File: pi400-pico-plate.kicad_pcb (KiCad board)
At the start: 2 copper layers, 44 x 52.5 mm, 7 parts, among them J1 2.54mm socket RA, J2 2.54mm header, J3 2.54mm header, J4 2.54mm header, J5 2.54mm header, SW1 PTS815, U1 Pico

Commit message: Start rev B changes -- make UART jumpers cut-link, remove aux GND header
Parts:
- removed J5: 2.54mm header, Connector_PinHeader_2.54mm:PinHeader_2x01_P2.54mm_Vertical
- J2, J4: value 2.54mm header -> 2.54mm jumper cut-link; footprint Connector_PinHeader_2.54mm:PinHeader_2x01_P2.54mm_Vertical -> pi400-pico-plate:2.54mm- jumper-closed
- J3: footprint Connector_PinHeader_2.54mm:PinHeader_2x01_P2.54mm_Vertical -> pi400-pico-plate:PinHeader_2x01_P2.54mm_Vertical
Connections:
- J1 pad 14: unconnected-(J1-Pad14) -> GND
- J1 pad 25: unconnected-(J1-Pad25) -> GND
- J1 pad 30: unconnected-(J1-Pad30) -> GND
- U1 pad 13: unconnected-(U1-Pad13) -> GND
- U1 pad 33: unconnected-(U1-Pad33) -> GND
- U1 pad 8: unconnected-(U1-Pad8) -> GND
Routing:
- net GND: vias 24 -> 28
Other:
- board text added: "JLCJLCJLCJLC"

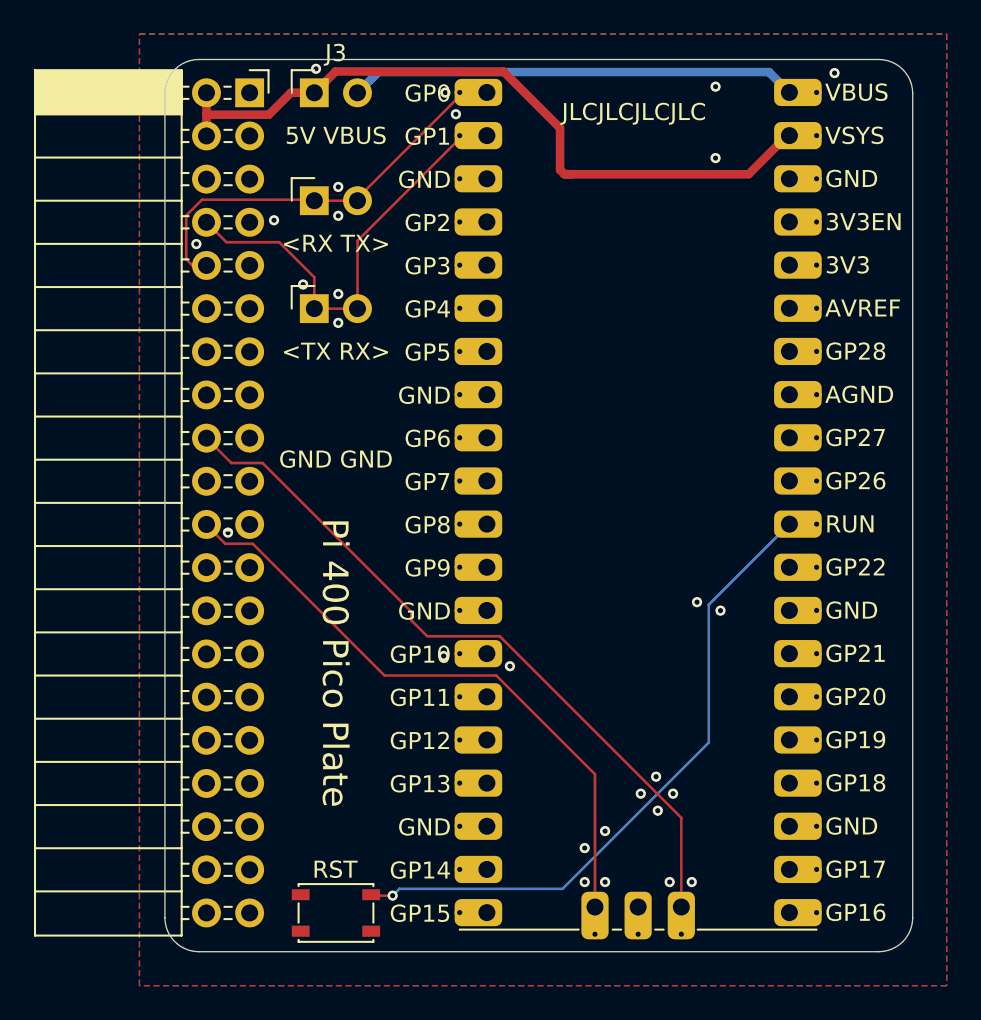
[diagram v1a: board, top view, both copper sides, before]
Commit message: Add indicator LEDs, trim bottom board edge by 0.5 mm (by Pico SWD pads)
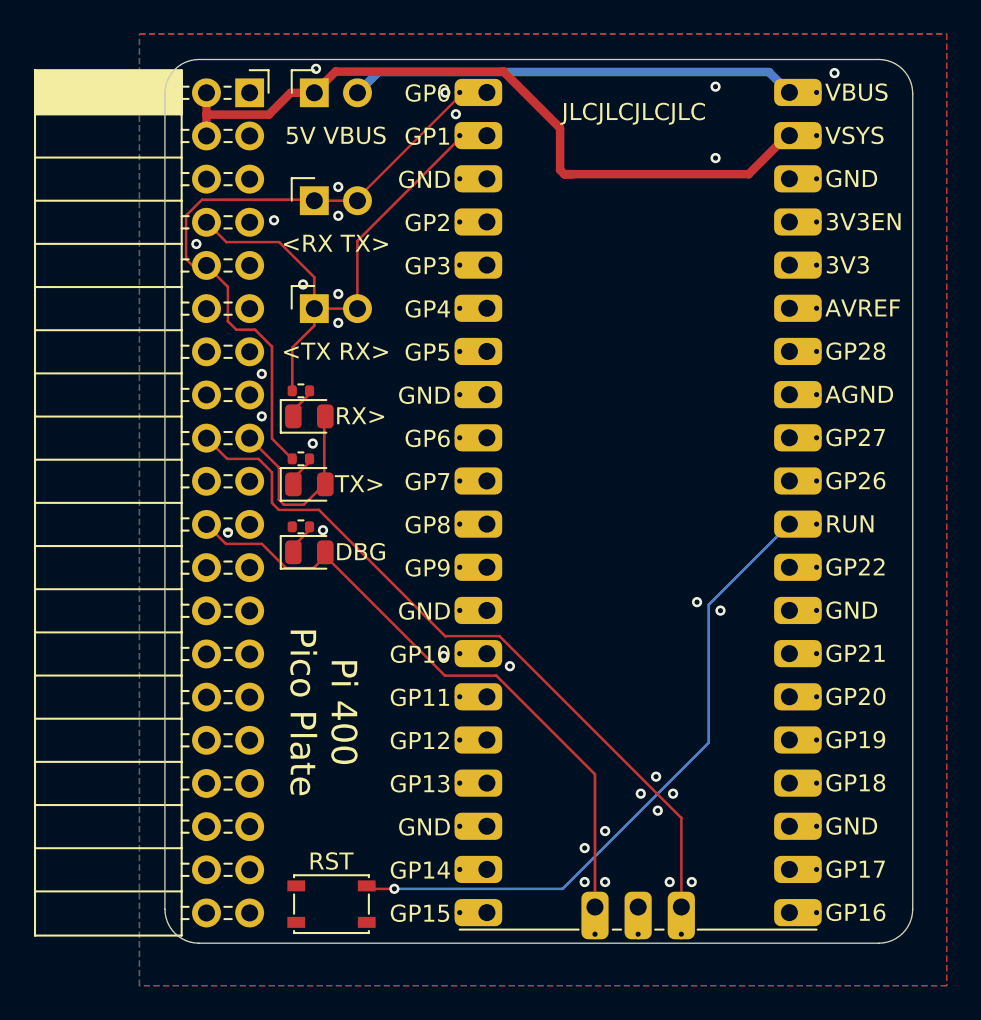
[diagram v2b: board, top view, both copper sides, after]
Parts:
- added D1: LED, LED_SMD:LED_0805_2012Metric, F.Cu at (137.5, 80.0)
- added D2: LED, LED_SMD:LED_0805_2012Metric, F.Cu at (137.5, 84.0)
- added D3: LED, LED_SMD:LED_0805_2012Metric, F.Cu at (137.5, 88.0)
- added R1: 2k2, Resistor_SMD:R_0402_1005Metric, F.Cu at (137.0, 78.5)
- added R2: 2k2, Resistor_SMD:R_0402_1005Metric, F.Cu at (137.0, 82.5)
- added R3: 2k2, Resistor_SMD:R_0402_1005Metric, F.Cu at (137.0, 86.5)
- moved SW1 0.58 mm to (138.8, 108.7)
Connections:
- J1 pad 17: unconnected-(J1-Pad17) -> +3V3
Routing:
- net /PI_UART_RX: track 11.9 -> 26.0 mm
- net +3V3: track 0.00 -> 11.7 mm
- net /PI_UART_TX: track 9.53 -> 14.9 mm
- net Net-(D2-Pad1): track 0.00 -> 1.92 mm
- net Net-(D3-Pad1): track 0.00 -> 1.89 mm
- net Net-(D1-Pad1): track 0.00 -> 1.89 mm
- net /SWCLK: track 36.8 -> 37.8 mm
- net /SWDIO: track 42.7 -> 43.5 mm
- net GND: vias 28 -> 32
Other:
- board size 44 x 52.5 mm -> 44 x 52 mm
- board text added: "DBG"
- board text added: "RX>"
- board text added: "Rev B"
- board text added: "TX>"
- board text added: "github.com/wren6991/pi400-pico-plate"
- board text removed: "GND GND"

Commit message: Add mounting holes for standoffs. Power layout changed as a result
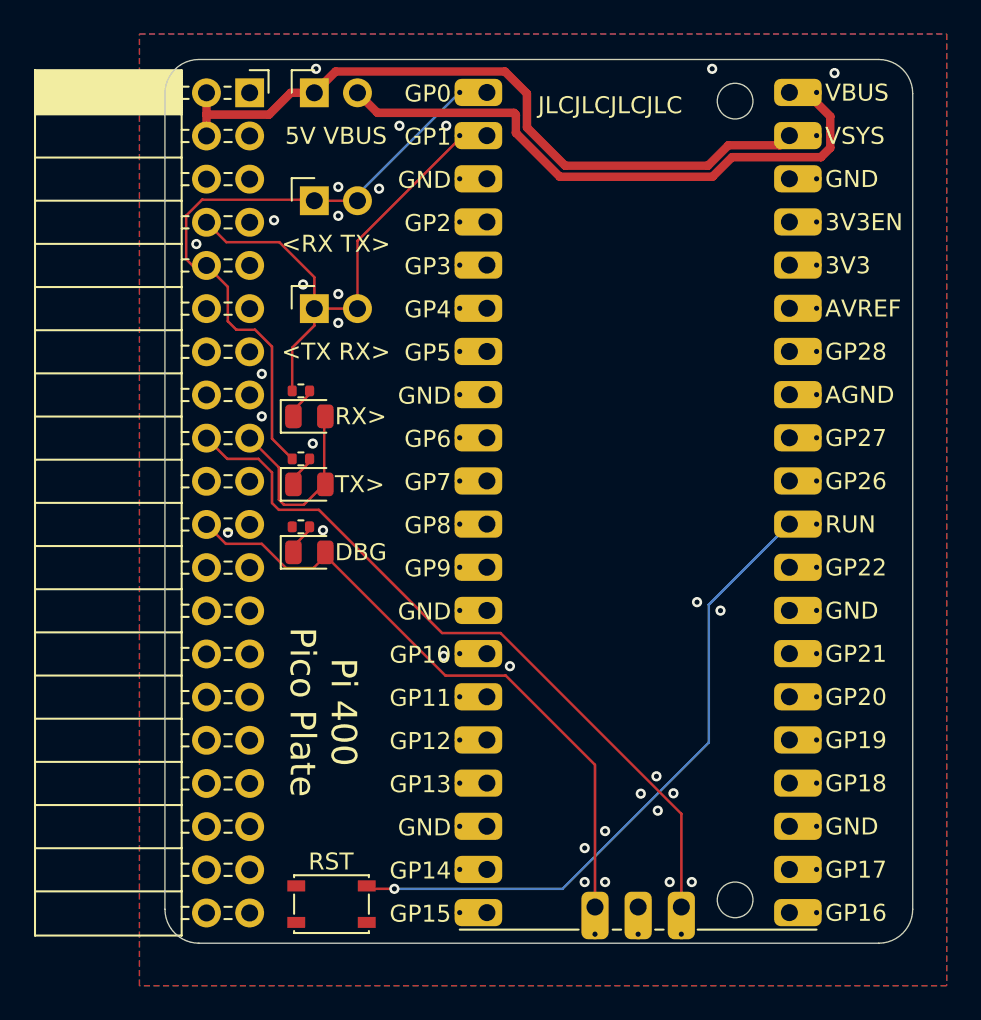
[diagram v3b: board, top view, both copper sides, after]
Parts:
- added REF**: MH_Pico_M2ish, pi400-pico-plate:MH_Pico_M2ish, F.Cu at (162.6, 61.5)
- added REF**: MH_Pico_M2ish, pi400-pico-plate:MH_Pico_M2ish, F.Cu at (162.6, 108.5)
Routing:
- net VBUS: track 26.4 -> 36.0 mm
- net +5V: track 43.3 -> 42.1 mm
